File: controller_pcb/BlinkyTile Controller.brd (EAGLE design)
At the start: 40 x 25 mm, 29 parts, among them CON1 USB_MICROSMT+THRUHULE, Q1 16MHz, U1 MK20D--VFM5, U2 W25Q--DVSS(208), U3 74LVC1G17DCK, U4 74LVC1G17DCK, U5 74LVC1G17DCK, U6 TPD4S012

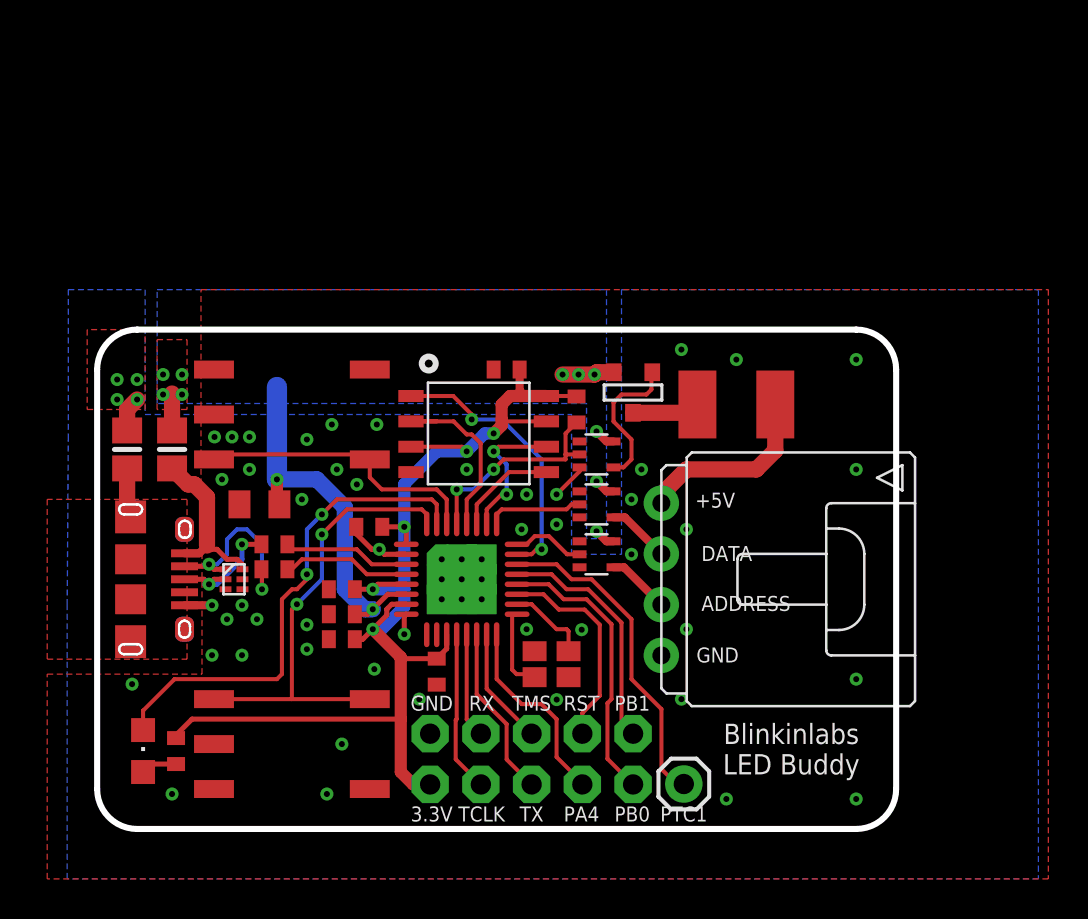
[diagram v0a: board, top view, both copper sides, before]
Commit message: Add protection diode, JST battery connector, tweak positions for manufacturability, redo silk
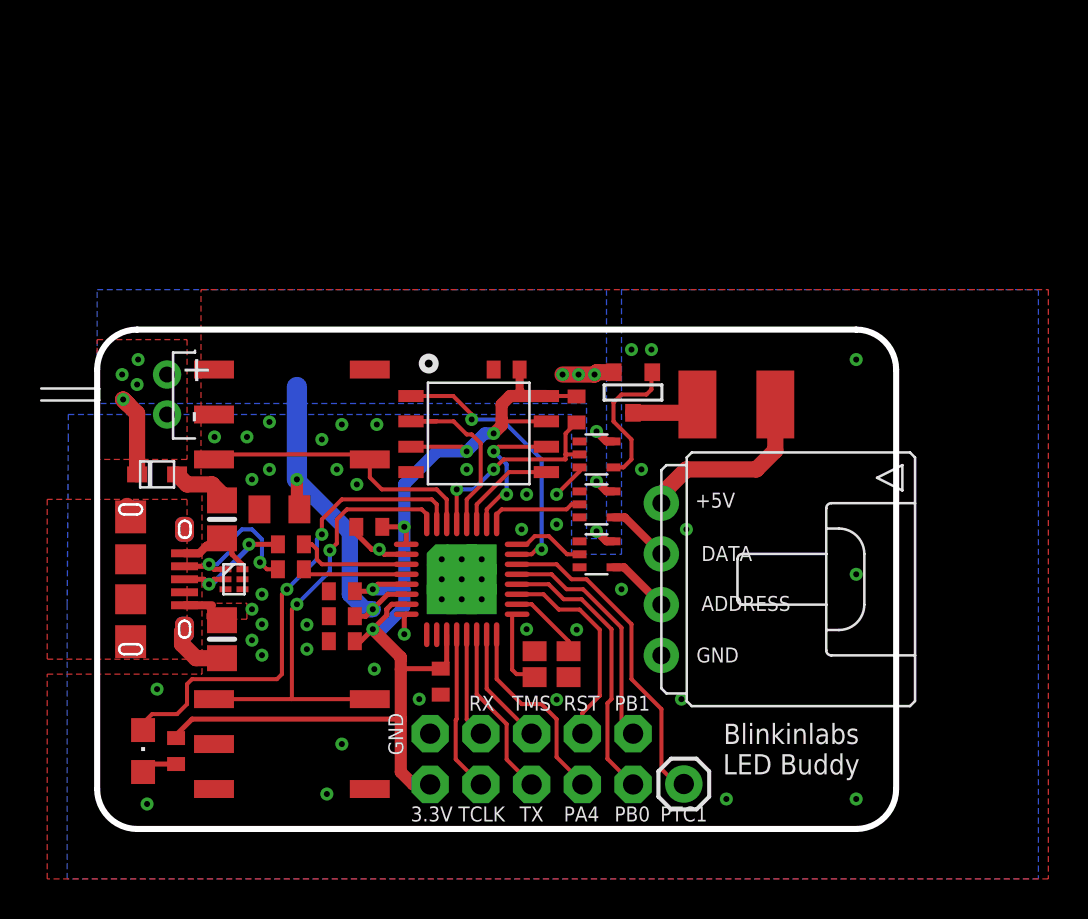
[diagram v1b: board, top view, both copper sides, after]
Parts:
- added CN1: (no value), adafruit:JST-PH-2-THM-RA
- added D1: (no value), adafruit:SOD-323F
- moved L2 10.6 mm to (6.25, -3.00)
- moved L3 4.30 mm to (6.25, 3.00)
- moved C8 1.03 mm to (9.12, 3.50)
- moved R1 0.82 mm to (9.70, 0.50)
- moved R2 0.82 mm to (9.70, 1.75)
- moved C6 0.54 mm to (17.2, -5.12)
- moved C2 0.10 mm to (12.2, -3.10)
- moved C3 0.10 mm to (12.2, -1.85)
- moved C4 0.10 mm to (12.2, -0.60)
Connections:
- new net N$9: D1.A, L3.1
- net +5V: now also CN1.1, D1.C; no longer L3.1
- net GND: now also CN1.2
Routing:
- net N$3: track 8.46 -> 4.16 mm
- net N$9: track 0.00 -> 2.96 mm
- net GND: track 9.27 -> 7.52 mm, vias 52 -> 43
- net +5V: track 26.4 -> 28.0 mm
- net N$7: track 9.58 -> 8.31 mm
- net N$11: track 6.47 -> 5.23 mm
- net SHIELD: track 2.12 -> 3.34 mm
- net +3V3: track 61.1 -> 61.8 mm
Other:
- board text added: "Blinkinlabs LED Buddy Rev D Blinkinlabs.com"
- board text removed: "Blinkinlabs LED Buddy Rev C Blinkinlabs.com"

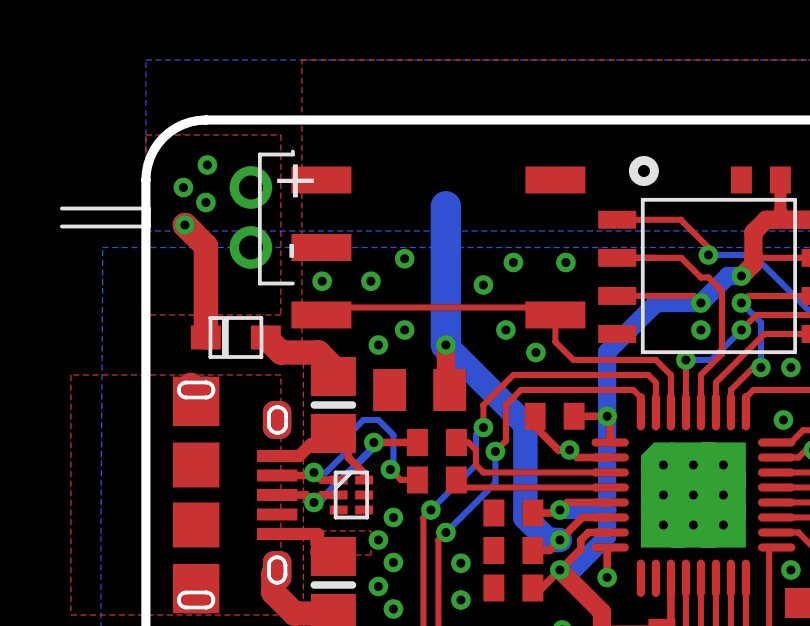
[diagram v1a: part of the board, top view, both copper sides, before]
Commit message: Clean up schematic layout
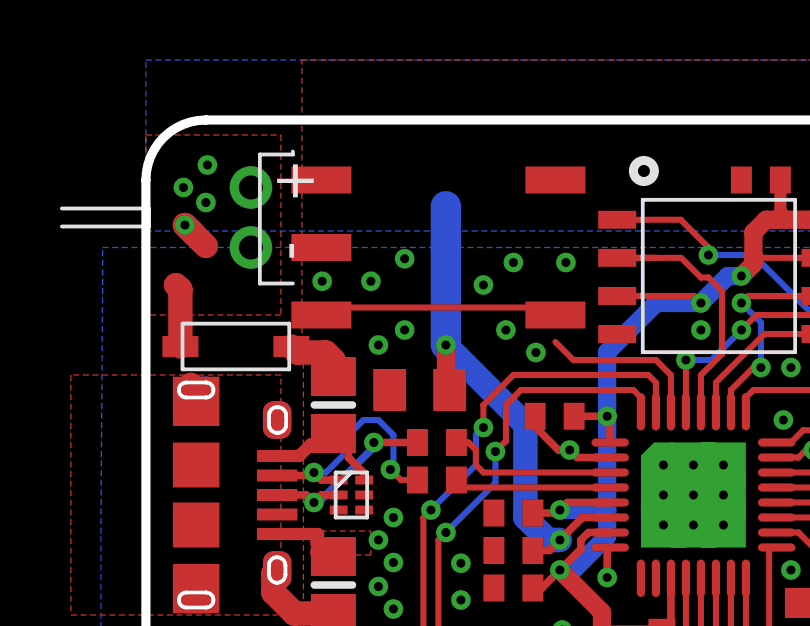
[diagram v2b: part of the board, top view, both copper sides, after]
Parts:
- removed D1: (no value), adafruit:SOD-323F
- added D3: RB161M-20, adafruit:SOD-123
- CN1: value (none) -> Battery
- R5: value 10k -> 1k
- SV1: value (none) -> LED_OUT
- T1: value (none) -> SSM3J328R,LF
- U$1: value BUTTON_MOMENTARY_GROUND -> BUTTON_1
- U$2: value BUTTON_MOMENTARY_GROUND -> BUTTON_2
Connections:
- net SW1 renamed BUTTON1
- new net BUTTON2: U$2.1, U$2.2
- net +5V: now also D3.C; no longer D1.C
- net N$9: now also D3.A; no longer D1.A
- net SW2: no longer U$2.1, U$2.2
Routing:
- net SW2: track 14.4 -> 5.53 mm
- net BUTTON2: track 0.00 -> 8.30 mm
- net +5V: track 28.0 -> 27.1 mm
- net N$9: track 2.96 -> 2.14 mm
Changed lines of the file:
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@@
 <setting verticaltext="up"/>
 </settings>
-<grid distance="0.000943" unitdist="inch" unit="inch" style="lines" multiple="1" display="yes" altdistance="0.25" altunitdist="mm" altunit="mm"/>
+<grid distance="1" unitdist="mm" unit="mm" style="lines" multiple="1" display="yes" altdistance="0.25" altunitdist="mm" altunit="mm"/>
 <layers>
 <layer number="1" name="Top" color="4" fill="1" visible="yes" active="yes"/>
@@
 <layer number="18" name="Vias" color="2" fill="1" visible="yes" active="yes"/>
 <layer number="19" name="Unrouted" color="6" fill="1" visible="yes" active="yes"/>
-<layer number="20" name="Dimension" color="15" fill="1" visible="yes" active="yes"/>
-<layer number="21" name="tPlace" color="7" fill="1" visible="yes" active="yes"/>
-<layer number="22" name="bPlace" color="7" fill="1" visible="yes" active="yes"/>
-<layer number="23" name="tOrigins" color="15" fill="1" visible="yes" active="yes"/>
-<layer number="24" name="bOrigins" color="15" fill="1" visible="yes" active="yes"/>
+<layer number="20" name="Dimension" color="15" fill="1" visible="no" active="yes"/>
+<layer number="21" name="tPlace" color="7" fill="1" visible="no" active="yes"/>
+<layer number="22" name="bPlace" color="7" fill="1" visible="no" active="yes"/>
+<layer number="23" name="tOrigins" color="15" fill="1" visible="no" active="yes"/>
+<layer number="24" name="bOrigins" color="15" fill="1" visible="no" active="yes"/>
 <layer number="25" name="tNames" color="7" fill="1" visible="no" active="yes"/>
 <layer number="26" name="bNames" color="7" fill="1" visible="no" active="yes"/>
@@
 <layer number="45" name="Holes" color="7" fill="1" visible="no" active="yes"/>
 <layer number="46" name="Milling" color="3" fill="1" visible="no" active="yes"/>
-<layer number="47" name="Measures" color="7" fill="1" visible="yes" active="yes"/>
-<layer number="48" name="Document" color="7" fill="1" visible="yes" active="yes"/>
+<layer number="47" name="Measures" color="7" fill="1" visible="no" active="yes"/>
+<layer number="48" name="Document" color="7" fill="1" visible="no" active="yes"/>
 <layer number="49" name="Reference" color="7" fill="1" visible="no" active="yes"/>
 <layer number="50" name="dxf" color="7" fill="1" visible="no" active="no"/>
-<layer number="51" name="tDocu" color="7" fill="1" visible="yes" active="yes"/>
+<layer number="51" name="tDocu" color="7" fill="1" visible="no" active="yes"/>
 <layer number="52" name="bDocu" color="7" fill="1" visible="no" active="yes"/>
 <layer number="53" name="tGND_GNDA" color="7" fill="9" visible="no" active="no"/>
@@
 <element name="U5" library="74xx-little-us" package="SC70-5" value="74LVC1G17DCK" x="25" y="1.25" smashed="yes" rot="R270"/>
 <element name="U3" library="74xx-little-us" package="SC70-5" value="74LVC1G17DCK" x="25" y="6.25" smashed="yes" rot="R270"/>
-<element name="T1" library="zetex" package="SOT-23" value="" x="26.8" y="9.35" smashed="yes">
+<element name="T1" library="zetex" package="SOT-23" value="SSM3J328R,LF" x="26.8" y="9.35" smashed="yes">
 <attribute name="OC_NEWARK" value="unknown" x="26.8" y="9.35" size="1.778" layer="27" display="off"/>
 <attribute name="MPN" value="" x="26.8" y="9.35" size="1.778" layer="27" display="off"/>
@@
 <attribute name="VALUE" x="15.295" y="-4.49" size="1.27" layer="27" rot="R270"/>
 </element>
-<element name="R5" library="adafruit" package="R0402" value="10k" x="24" y="8.5" smashed="yes" rot="R90">
+<element name="R5" library="adafruit" package="R0402" value="1k" x="24" y="8.5" smashed="yes" rot="R90">
 <attribute name="VALUE" x="26.032" y="7.865" size="1.27" layer="27" rot="R90"/>
 </element>
-<element name="SV1" library="blinkinlabs" package="DUPONT-4P" value="" x="28.246" y="0" smashed="yes" rot="R270">
+<element name="SV1" library="blinkinlabs" package="DUPONT-4P" value="LED_OUT" x="28.246" y="0" smashed="yes" rot="R270">
 <attribute name="VALUE" x="29.897" y="-0.635" size="1.27" layer="27" ratio="10" rot="R270"/>
 </element>
@@
 <attribute name="VALUE" x="28.1" y="-13.425" size="1.27" layer="27"/>
 </element>
-<element name="U$1" library="blinkinlabs" package="TD-07XB" value="BUTTON_MOMENTARY_GROUND" x="9.75" y="-8.25" smashed="yes">
+<element name="U$1" library="blinkinlabs" package="TD-07XB" value="BUTTON_1" x="9.75" y="-8.25" smashed="yes">
 <attribute name="VALUE" x="6.915" y="-13.425" size="1.27" layer="27"/>
 </element>
-<element name="U$2" library="blinkinlabs" package="TD-07XB" value="BUTTON_MOMENTARY_GROUND" x="9.75" y="8.25" smashed="yes">
+<element name="U$2" library="blinkinlabs" package="TD-07XB" value="BUTTON_2" x="9.75" y="8.25" smashed="yes">
 <attribute name="VALUE" x="6.915" y="3.075" size="1.27" layer="27"/>
 </element>
@@
 <attribute name="VALUE" x="7.012" y="-0.968" size="0.4064" layer="27" ratio="10" rot="R90"/>
 </element>
-<element name="CN1" library="adafruit" package="JST-PH-2-THM-RA" value="" x="3.5" y="9.25" smashed="yes" rot="R90"/>
-<element name="D1" library="adafruit" package="SOD-323F" value="" x="3" y="5.25" smashed="yes" rot="R180">
-<attribute name="VALUE" x="5.1" y="6.95" size="0.8128" layer="27" font="vector" rot="R180"/>
+<element name="CN1" library="adafruit" package="JST-PH-2-THM-RA" value="Battery" x="3.5" y="9.25" smashed="yes" rot="R90"/>
+<element name="D3" library="adafruit" package="SOD-123" value="RB161M-20" x="3" y="4.95" smashed="yes">
+<attribute name="VALUE" x="1.9" y="3.666" size="0.4064" layer="27"/>
 </element>
 </elements>
@@
 <contactref element="CN1" pad="1"/>
 <wire x1="1.55" y1="8.75" x2="1.3" y2="9" width="0.8128" layer="1"/>
-<contactref element="D1" pad="C"/>
-<wire x1="2" y1="5.25" x2="2" y2="8.3" width="0.8128" layer="1"/>
 <wire x1="2" y1="8.3" x2="1.3" y2="9" width="0.8128" layer="1"/>
 <wire x1="12.9" y1="-1.85" x2="13.45" y2="-1.85" width="0.254" layer="1"/>
 <wire x1="13.45" y1="-1.85" x2="13.8" y2="-1.5" width="0.254" layer="1"/>
+<contactref element="D3" pad="C"/>
+<wire x1="1.15" y1="4.95" x2="1.15" y2="6.85" width="0.8128" layer="1"/>
+<wire x1="1.15" y1="6.85" x2="1" y2="7" width="0.8128" layer="1"/>
 </signal>
 <signal name="+3V3">
@@
 <wire x1="6.75" y1="1.55" x2="6.25" y2="2.05" width="0.254" layer="1"/>
 </signal>
-<signal name="SW1">
+<signal name="BUTTON1">
 <via x="10" y="-1.25" extent="1-16" drill="0.3"/>
 <contactref element="U1" pad="32"/>
@@
 <wire x1="17.5" y1="3.996" x2="16.996" y2="4.5" width="0.2032" layer="1"/>
 <wire x1="16.996" y1="4.5" x2="14.25" y2="4.5" width="0.2032" layer="1"/>
-<contactref element="U$2" pad="1"/>
-<contactref element="U$2" pad="2"/>
 <wire x1="14.25" y1="4.5" x2="13.65" y2="5.1" width="0.2032" layer="1"/>
-<wire x1="13.65" y1="6" x2="13.65" y2="5.1" width="0.2032" layer="1"/>
-<wire x1="13.65" y1="6" x2="13.25" y2="6" width="0.2032" layer="1"/>
-<wire x1="13.25" y1="6" x2="13" y2="6.25" width="0.2032" layer="1"/>
-<wire x1="13" y1="6.25" x2="6.1" y2="6.25" width="0.2032" layer="1"/>
-<wire x1="6.1" y1="6.25" x2="5.85" y2="6" width="0.2032" layer="1"/>
 </signal>
 <signal name="DATA_OUT">
@@
 </signal>
 <signal name="N$9">
-<contactref element="D1" pad="A"/>
 <contactref element="L3" pad="1"/>
-<wire x1="6.25" y1="3.95" x2="6.25" y2="4.25" width="0.8128" layer="1"/>
-<wire x1="6.25" y1="4.25" x2="5.75" y2="4.75" width="0.8128" layer="1"/>
-<wire x1="5.75" y1="4.75" x2="4.5" y2="4.75" width="0.8128" layer="1"/>
-<wire x1="4.5" y1="4.75" x2="4" y2="5.25" width="0.8128" layer="1"/>
+<contactref element="D3" pad="A"/>
+<wire x1="6.25" y1="3.95" x2="6.25" y2="4.5" width="0.8128" layer="1"/>
+<wire x1="6.25" y1="4.5" x2="6" y2="4.75" width="0.8128" layer="1"/>
+<wire x1="6" y1="4.75" x2="5.05" y2="4.75" width="0.8128" layer="1"/>
+<wire x1="5.05" y1="4.75" x2="4.85" y2="4.95" width="0.8128" layer="1"/>
+</signal>
+<signal name="BUTTON2">
+<contactref element="U$2" pad="1"/>
+<contactref element="U$2" pad="2"/>
+<wire x1="13.65" y1="6" x2="13" y2="6" width="0.2032" layer="1"/>
+<wire x1="13" y1="6" x2="13" y2="6.25" width="0.2032" layer="1"/>
+<wire x1="13" y1="6.25" x2="6.5" y2="6.25" width="0.2032" layer="1"/>
+<wire x1="6.5" y1="6.25" x2="6.5" y2="6" width="0.2032" layer="1"/>
+<wire x1="6.5" y1="6" x2="5.85" y2="6" width="0.2032" layer="1"/>
 </signal>
 </signals>

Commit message: Controller boar design, as released.
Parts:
- removed D3: RB161M-20, adafruit:SOD-123
- removed JP1: M05X2NO_SILK, SparkFun-Connectors:2X5_NOSILK
- removed JP3: M01PTH, SparkFun-Connectors:1X01
- removed SV1: LED_OUT, blinkinlabs:DUPONT-4P
- removed U$1: BUTTON_1, blinkinlabs:TD-07XB
- removed U$2: BUTTON_2, blinkinlabs:TD-07XB
- added CON2: M05X2NO_SILK, SparkFun-Connectors:2X5_NOSILK
- added CON3: LED_OUT, blinkinlabs:DUPONT-4P
- added CON4: M01PTH, SparkFun-Connectors:1X01
- added D1: RB161M-20, adafruit:SOD-123
- added SW1: BUTTON_1, blinkinlabs:TD-07XB
- added SW2: BUTTON_2, blinkinlabs:TD-07XB
- R4: value 330 -> 470
- moved T1 12.5 mm to (26.8, 21.9)
- moved C1 12.5 mm to (13.6, 15.1)
- moved C2 12.5 mm to (12.2, 9.40)
- moved C3 12.5 mm to (12.2, 10.7)
- moved C4 12.5 mm to (12.2, 11.9)
- moved C5 12.5 mm to (20.5, 23.0)
- moved C6 12.5 mm to (17.2, 7.38)
- moved C8 12.5 mm to (9.12, 16.0)
- moved CN1 12.5 mm to (3.50, 21.8)
- moved CON1 12.5 mm to (1.68, 12.5)
- moved L1 12.5 mm to (32.0, 21.2)
- moved L2 12.5 mm to (6.25, 9.50)
- moved L3 12.5 mm to (6.25, 15.5)
- moved LED1 12.5 mm to (2.30, 3.90)
- moved Q1 12.5 mm to (22.8, 8.25)
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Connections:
- net +3V3: now also CON2.1; no longer JP1.1
- net +5V: now also D1.C; no longer D3.C
- net ADC15: now also CON4.1; no longer JP3.1
- net BUTTON1: now also SW1.3, SW1.4; no longer U$1.3, U$1.4
- net BUTTON2: now also SW2.1, SW2.2; no longer U$2.1, U$2.2
- net GND: now also CON2.2, CON3.P$4, SW1.1, SW1.2, SW1.5, SW2.3, SW2.4, SW2.5; no longer JP1.2, SV1.P$4, U$1.1, U$1.2, U$1.5, U$2.3, U$2.4, U$2.5
- net LED_DATA: now also CON3.P$2; no longer SV1.P$2
- net N$4: now also CON3.P$3; no longer SV1.P$3
- net N$8: now also CON3.P$1; no longer SV1.P$1
- net N$9: now also D1.A; no longer D3.A
- net PA4: now also CON2.7; no longer JP1.7
- net PB0: now also CON2.9; no longer JP1.9
- net PB1: now also CON2.10; no longer JP1.10
- net RESET: now also CON2.8; no longer JP1.8
- net RX: now also CON2.4; no longer JP1.4
- net TCLK: now also CON2.3; no longer JP1.3
- net TMS: now also CON2.6; no longer JP1.6
- net TX: now also CON2.5; no longer JP1.5
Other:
- board text added: "CON3"
- board text removed: "3.3V"
- board text removed: "Blinkinlabs LED Buddy"
- board text removed: "PA4"
- board text removed: "PB0"
- board text removed: "PB1"
- board text removed: "PTC1"
- board text removed: "RST"
- board text removed: "RX"
- board text removed: "TCLK"
- board text removed: "TMS"
- board text removed: "TX"
